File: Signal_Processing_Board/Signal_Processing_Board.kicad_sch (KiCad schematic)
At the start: 37 parts, among them J1 Screw_Terminal_01x02, J10 Conn_01x01_Socket, J11 Conn_01x01_Socket, J12 Conn_01x01_Socket, J13 Conn_01x01_Socket, J14 Conn_01x01_Socket, J15 Screw_Terminal_01x03, J16 Screw_Terminal_01x03, J18 Conn_01x01_Socket, J19 Conn_01x01_Socket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

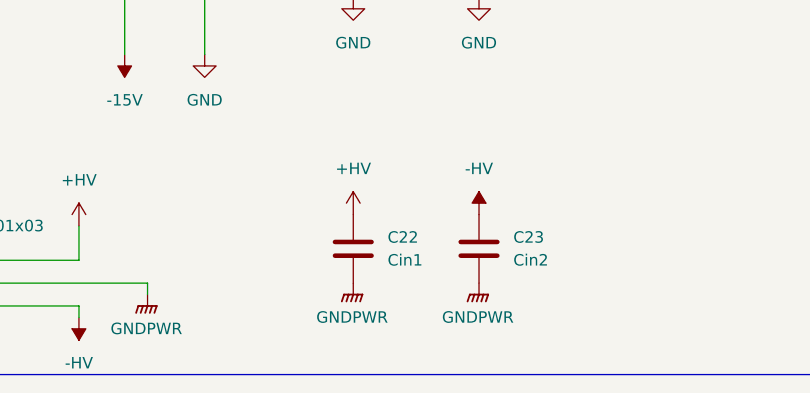
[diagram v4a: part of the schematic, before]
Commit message: Final version of the board, updated with lessons from first version
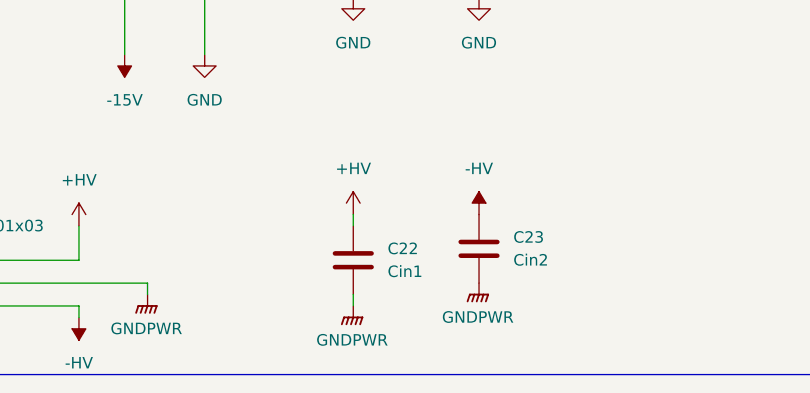
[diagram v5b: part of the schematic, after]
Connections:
- net -HV: now also C23.2; no longer C23.1
- net GNDPWR: now also C23.1; no longer C23.2
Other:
- moved on the sheet: C22, C23
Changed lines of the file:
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@@
 	(wire
 		(pts
+			(xy 77.47 271.78) (xy 77.47 273.05)
+		)
+		(stroke
+			(width 0)
+			(type default)
+		)
+	)
+	(wire
+		(pts
 			(xy 46.99 264.16) (xy 46.99 267.97)
 		)
@@
 	(wire
 		(pts
+			(xy 77.47 262.89) (xy 77.47 264.16)
+		)
+		(stroke
+			(width 0)
+			(type default)
+		)
+	)
+	(wire
+		(pts
 			(xy 250.19 208.28) (xy 250.19 214.63)
 		)
@@
 	(symbol
 		(lib_id "Device:C")
-		(at 77.47 266.7 0)
+		(at 77.47 267.97 0)
 		(unit 1)
 		(exclude_from_sim no)
@@
 		(fields_autoplaced yes)
 		(property "Reference" "C22"
-			(at 81.28 265.4299 0)
+			(at 81.28 266.6999 0)
 			(effects
 				(font
@@
 		)
 		(property "Value" "Cin1"
-			(at 81.28 267.9699 0)
+			(at 81.28 269.2399 0)
 			(effects
 				(font
@@
 		)
 		(property "Footprint" "Capacitor_THT:CP_Radial_D10.0mm_P5.00mm"
-			(at 78.4352 270.51 0)
+			(at 78.4352 271.78 0)
 			(effects
 				(font
@@
 		)
 		(property "Datasheet" "~"
-			(at 77.47 266.7 0)
+			(at 77.47 267.97 0)
 			(effects
 				(font
@@
 		)
 		(property "Description" "Unpolarized capacitor"
-			(at 77.47 266.7 0)
+			(at 77.47 267.97 0)
 			(effects
 				(font
@@
 	(symbol
 		(lib_id "Device:C")
-		(at 91.44 266.7 0)
+		(at 91.44 266.7 180)
 		(unit 1)
 		(exclude_from_sim no)
@@
 					(size 1.27 1.27)
 				)
-				(justify left)
+				(justify right)
 			)
 		)
@@
 					(size 1.27 1.27)
 				)
-				(justify left)
+				(justify right)
 			)
 		)
 		(property "Footprint" "Capacitor_THT:CP_Radial_D10.0mm_P5.00mm"
-			(at 92.4052 270.51 0)
+			(at 90.4748 262.89 0)
 			(effects
 				(font
@@
 	(symbol
 		(lib_id "power:GNDPWR")
-		(at 77.47 270.51 0)
+		(at 77.47 273.05 0)
 		(unit 1)
 		(exclude_from_sim no)
@@
 		(fields_autoplaced yes)
 		(property "Reference" "#PWR066"
-			(at 77.47 275.59 0)
+			(at 77.47 278.13 0)
 			(effects
 				(font
@@
 		)
 		(property "Value" "GNDPWR"
-			(at 77.343 274.32 0)
+			(at 77.343 276.86 0)
 			(effects
 				(font
@@
 		)
 		(property "Footprint" ""
-			(at 77.47 271.78 0)
+			(at 77.47 274.32 0)
 			(effects
 				(font
@@
 		)
 		(property "Datasheet" ""
-			(at 77.47 271.78 0)
+			(at 77.47 274.32 0)
 			(effects
 				(font
@@
 		)
 		(property "Description" "Power symbol creates a global label with name \"GNDPWR\" , global ground"
-			(at 77.47 270.51 0)
+			(at 77.47 273.05 0)
 			(effects
 				(font

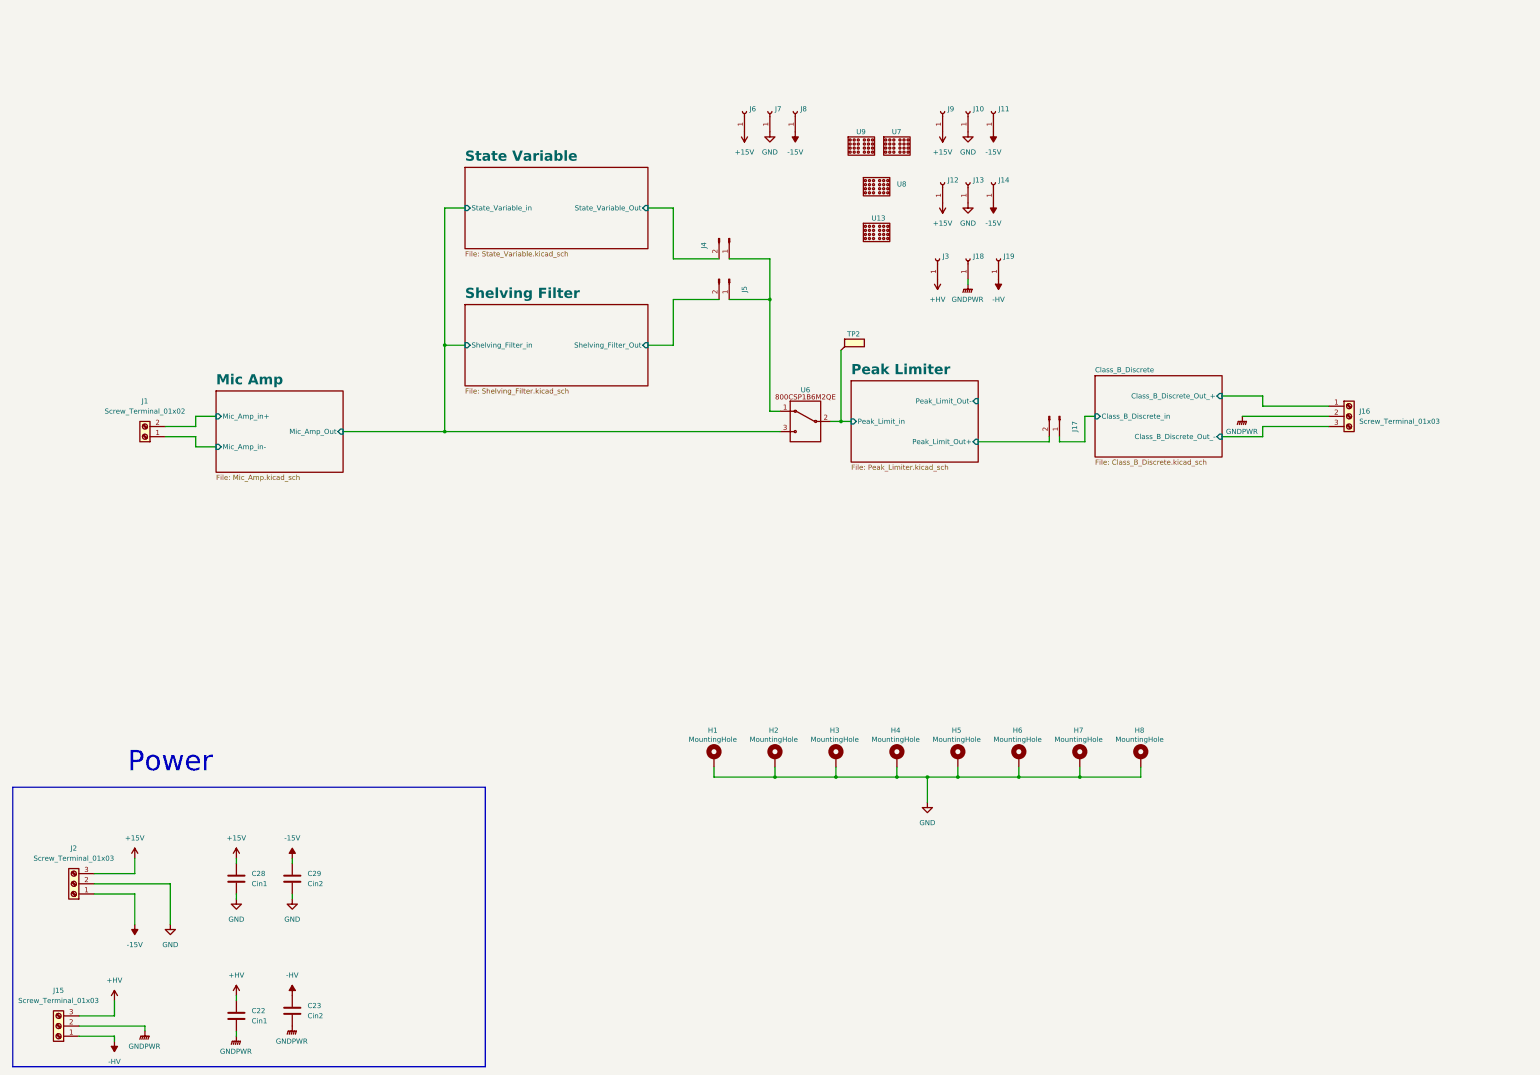
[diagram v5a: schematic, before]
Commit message: Updated file structure and added PDF of schematic
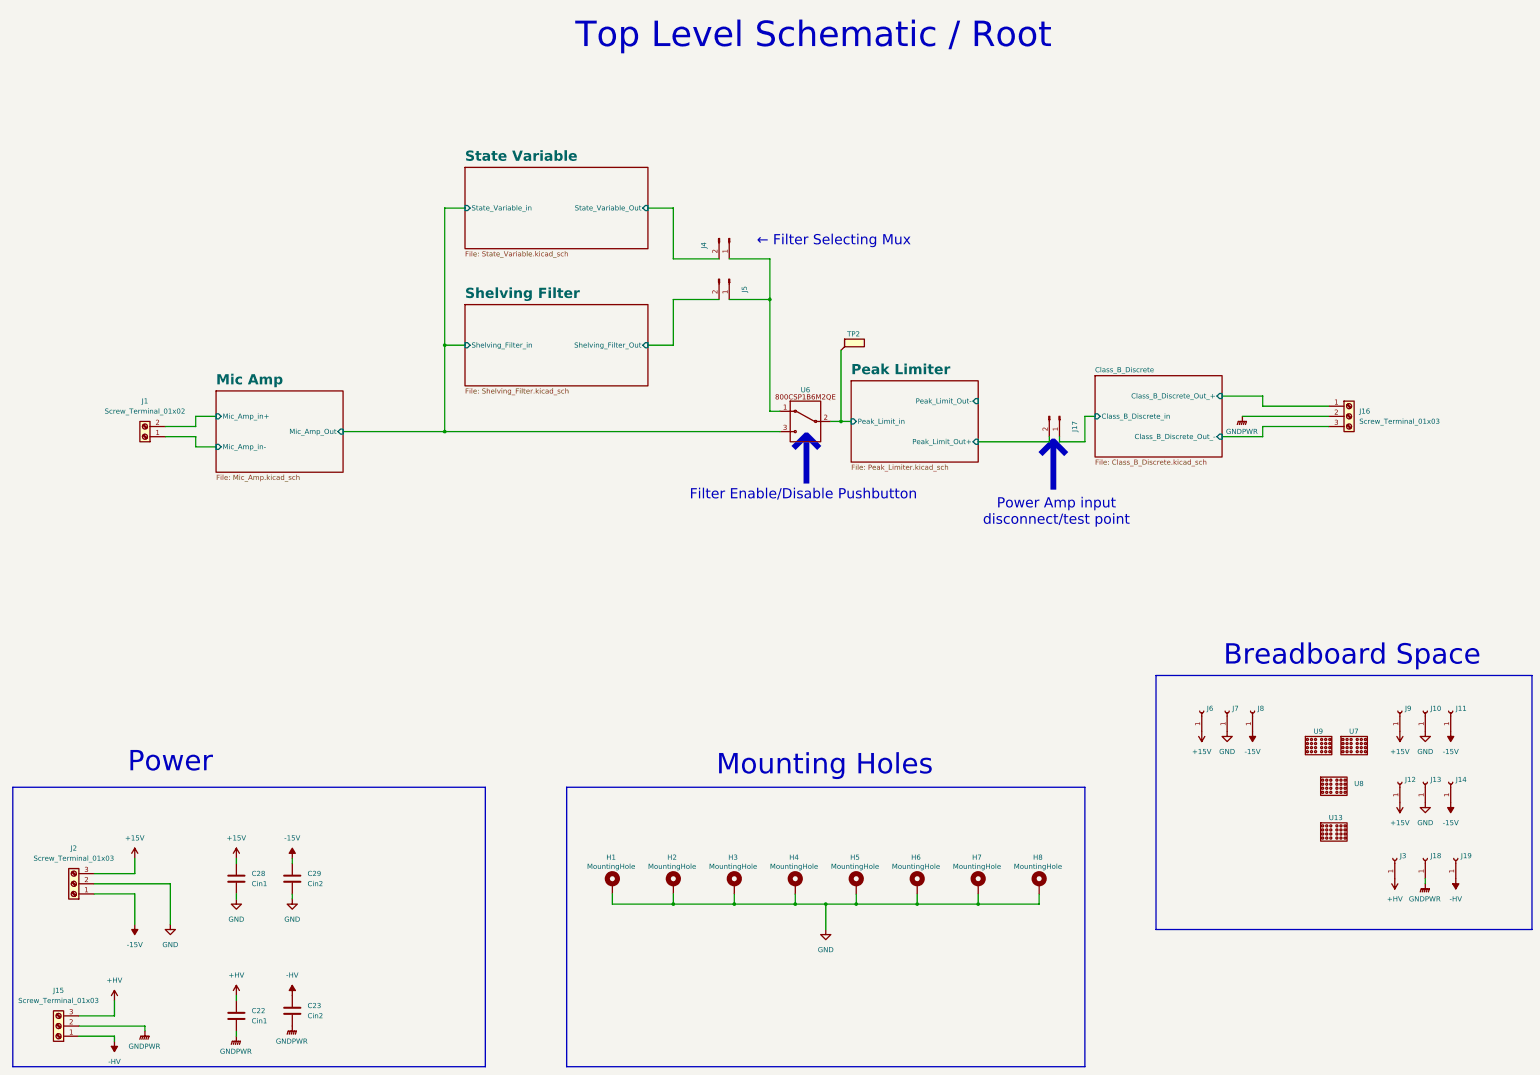
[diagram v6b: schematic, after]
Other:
- note added: "Breadboard Space"
- note added: "Filter Enable/Disable Pushbutton"
- note added: "Mounting Holes"
- note added: "Power Amp input disconnect/test point"
- note added: "Top Level Schematic / Root"
- note added: "← Filter Selecting Mux"
- note added: "↑"
- moved on the sheet: H1, H2, H3, H4, H5, H6, H7, H8, J10, J11, J12, J13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
